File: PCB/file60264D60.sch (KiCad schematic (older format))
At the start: 43 parts, among them J8 PJ-102AH, Q1 FDD6685, Q2 2N7002K, SW0 B3F-1055, U1 LMZ22005TZ_NOPB

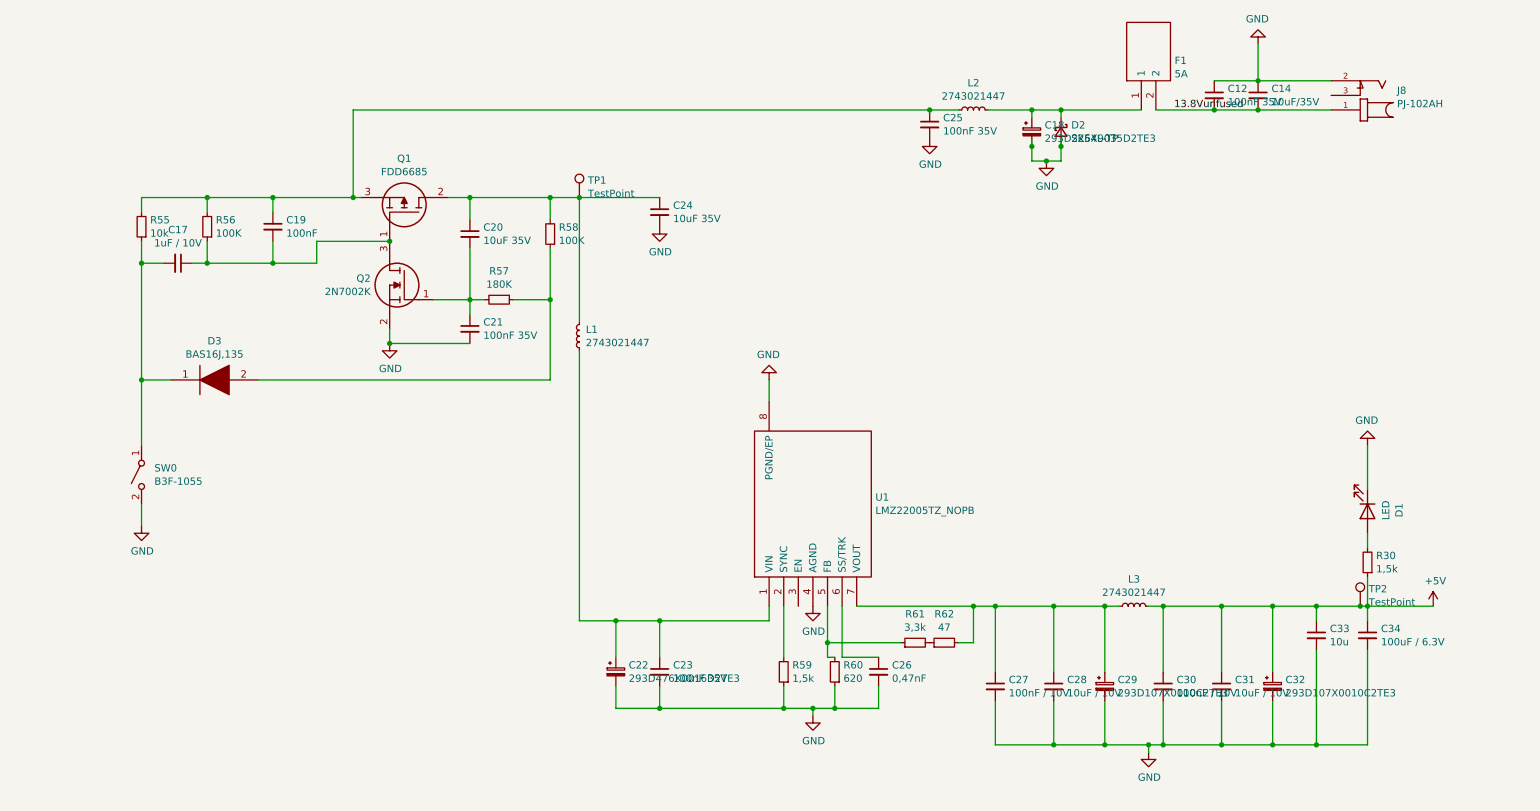
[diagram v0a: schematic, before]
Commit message: Cleaned up repository. Created a BOM in iBOM Format.
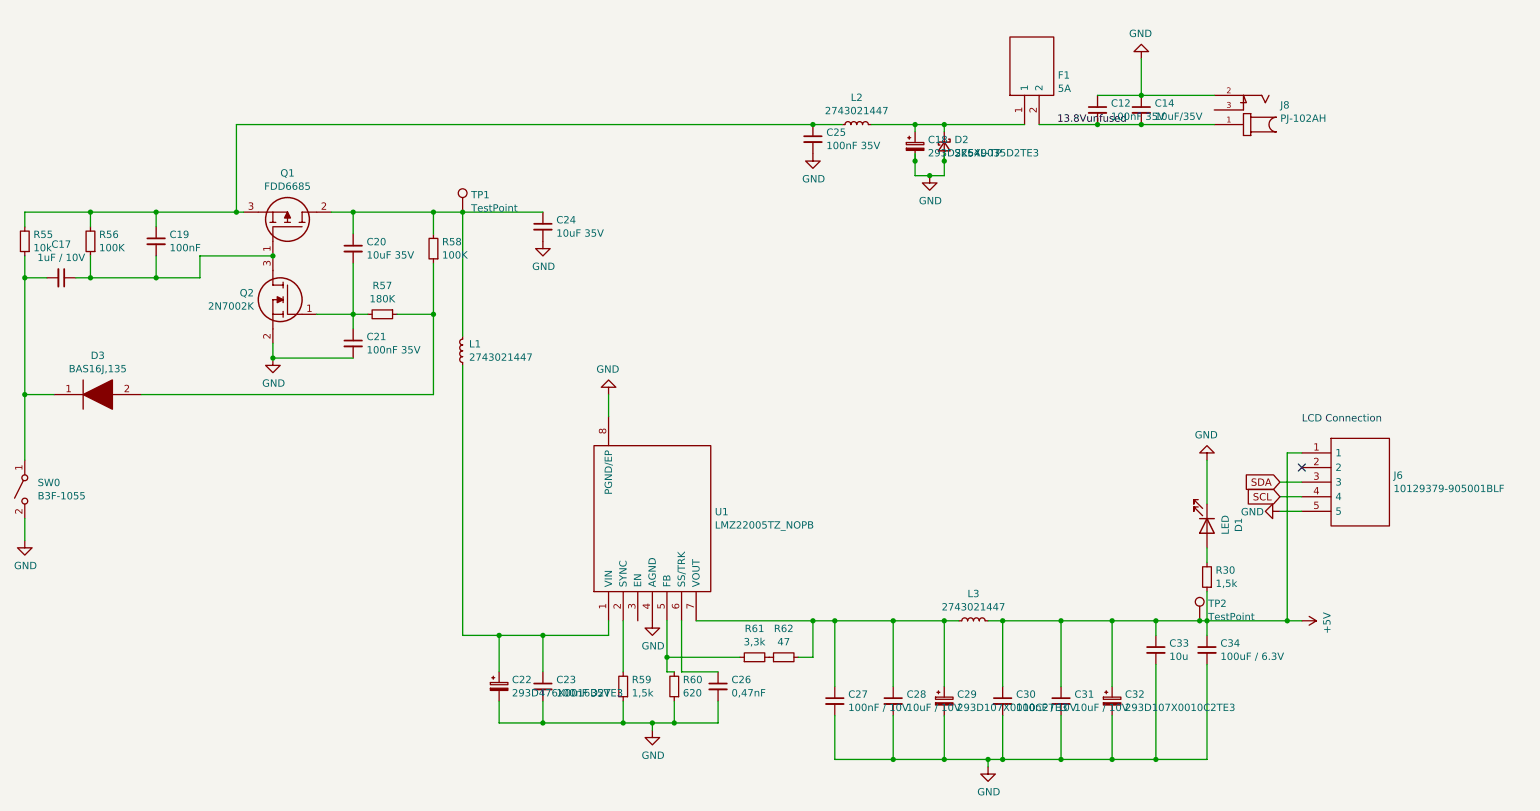
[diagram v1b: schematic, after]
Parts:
- added J6: 10129379-905001BLF, HDRRA5W67P0X254_1X5_1270X254X241P, symbol SamacSys_Parts:10129379-905001BLF
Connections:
- net +5V: now also J6.1
- net GND: now also J6.5
- new net SCL: J6.4
- new net SDA: J6.3
- no-connect marks 0 -> 1
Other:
- note added: "LCD Connection"
- moved on the sheet: C12, C14, C17, C18, C19, C20, C21, C22, C23, C24, C25, C26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

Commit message: Completed parts details on schematics and recreated gerbers and bom.
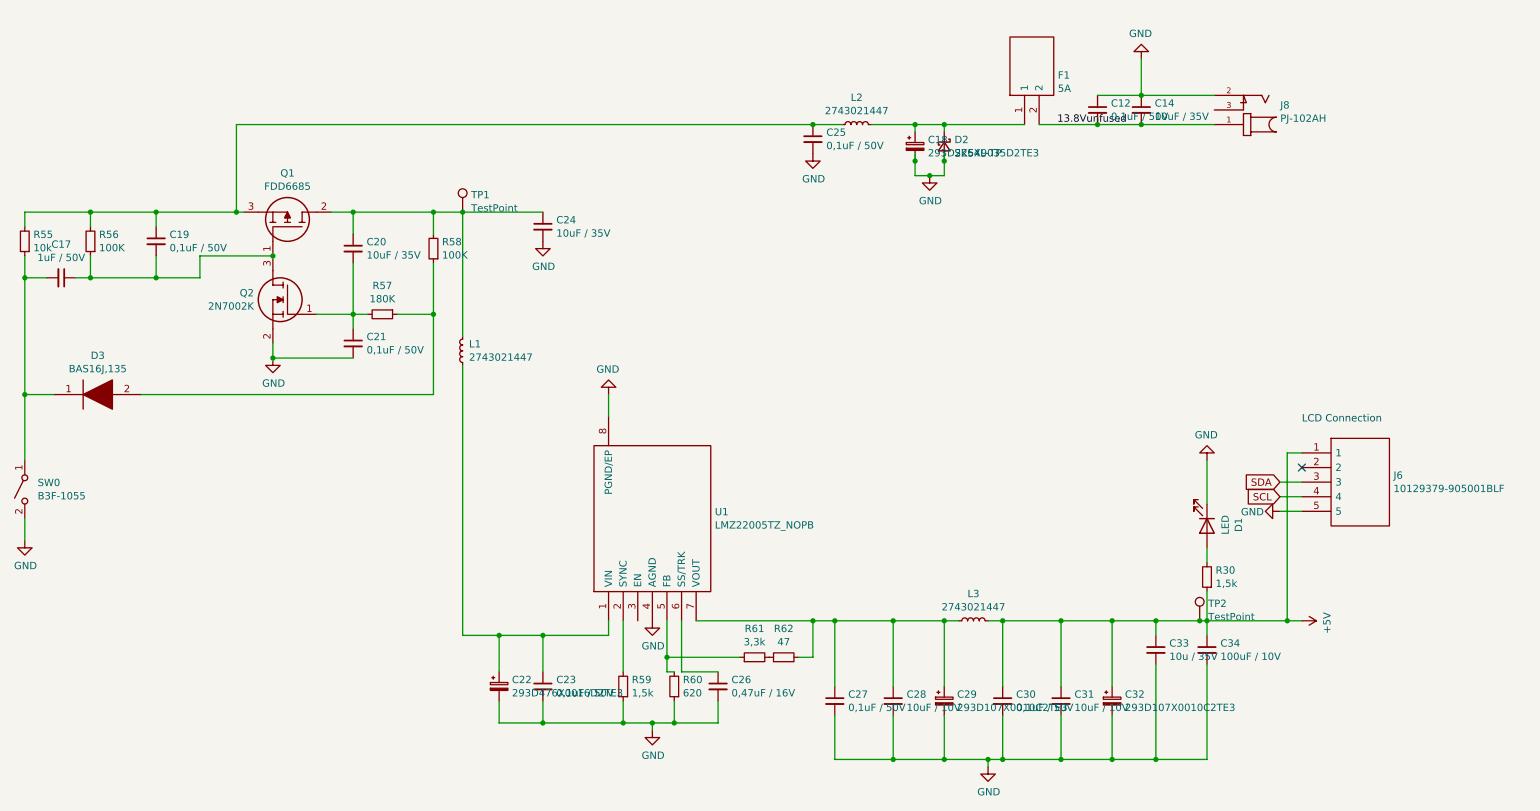
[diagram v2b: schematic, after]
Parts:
- C12, C21, C23, C25: value 100nF 35V -> 0,1uF / 50V; LCSC (none) -> C62912; Manufacturer_Name (none) -> Samsung Electro-Mechanics; Manufacturer_Part_Number (none) -> CL21B104KBCSFNC; Mouser Part Number (none) -> 187-CL21B104KBCSFNC
- C14: value 10uF/35V -> 10uF / 35V; Manufacturer_Name (none) -> Samsung Electro-Mechanics; Manufacturer_Part_Number (none) -> CL21A106KBYQNNE; Mouser Part Number (none) -> 187-CL21A106KBYQNNE
- C17: value 1uF / 10V -> 1uF / 50V; LCSC (none) -> C28323; Manufacturer_Name (none) -> Samsung Electro-Mechanics; Manufacturer_Part_Number (none) -> CL21B105KBFNNNE; Mouser Part Number (none) -> 187-CL21B105KBFNNNE
- C18: LCSC (none) -> C167035
- C19: value 100nF -> 0,1uF / 50V; LCSC (none) -> C62912; Manufacturer_Name (none) -> Samsung Electro-Mechanics; Manufacturer_Part_Number (none) -> CL21B104KBCSFNC; Mouser Part Number (none) -> 187-CL21B104KBCSFNC
- C20, C24: value 10uF 35V -> 10uF / 35V; Manufacturer_Name (none) -> Samsung Electro-Mechanics; Manufacturer_Part_Number (none) -> CL21A106KBYQNNE; Mouser Part Number (none) -> 187-CL21A106KBYQNNE
- C22: LCSC (none) -> C130385
- C26: value 0,47nF -> 0,47uF / 16V; Manufacturer_Name (none) -> Samsung Electro-Mechanics; Manufacturer_Part_Number (none) -> CL21B474KOFNNNE; Mouser Part Number (none) -> 187-CL21B474KOFNNNE
- C27, C30: value 100nF / 10V -> 0,1uF / 50V; LCSC (none) -> C62912; Manufacturer_Name (none) -> Samsung Electro-Mechanics; Manufacturer_Part_Number (none) -> CL21B104KBCSFNC; Mouser Part Number (none) -> 187-CL21B104KBCSFNC
- C28, C31: LCSC (none) -> C91245; Manufacturer_Name (none) -> Samsung Electro-Mechanics; Manufacturer_Part_Number (none) -> CL21A106MPFNNNE; Mouser Part Number (none) -> 187-CL21A106MPFNNNE
- C29, C32: LCSC (none) -> C136005
- C33: value 10u -> 10u / 35V; Manufacturer_Name (none) -> Samsung Electro-Mechanics; Manufacturer_Part_Number (none) -> CL21A106KBYQNNE; Mouser Part Number (none) -> 187-CL21A106KBYQNNE
- C34: value 100uF / 6.3V -> 100uF / 10V; footprint Capacitor_SMD:C_1210_3225Metric_Pad1.42x2.65mm_HandSolder -> Capacitor_SMD:C_0805_2012Metric_Pad1.15x1.40mm_HandSolder; LCSC (none) -> C307523; Manufacturer_Name (none) -> Samsung Electro-Mechanics; Manufacturer_Part_Number (none) -> CL21A106KPFNNNG; Mouser Part Number (none) -> 187-CL21A106KPFNNNG
- J8: Manufacturer_Name (none) -> CUI Devices; Manufacturer_Part_Number (none) -> PJ-102AH; Mouser Part Number (none) -> 490-PJ-102AH
- Q1: LCSC (none) -> C10866
- Q2: LCSC (none) -> C116584
- R30, R59: LCSC (none) -> C4310; Manufacturer_Name (none) -> Vishay; Manufacturer_Part_Number (none) -> CRCW08051K50FKEA; Mouser Part Number (none) -> 71-CRCW0805-1.5K-E3
- R55: LCSC (none) -> C17414; Manufacturer_Name (none) -> Vishay; Manufacturer_Part_Number (none) -> CRCW080510K0FKEAC; Mouser Part Number (none) -> 71-CRCW080510K0FKEAC
- R56, R58: LCSC (none) -> C17407; Manufacturer_Name (none) -> Vishay; Manufacturer_Part_Number (none) -> CRCW0805100KFKEAC; Mouser Part Number (none) -> 71-CRCW0805100KFKEAC
- R57: LCSC (none) -> C17501; Manufacturer_Name (none) -> Vishay; Manufacturer_Part_Number (none) -> CRCW0805180KFKEAC; Mouser Part Number (none) -> 71-CRCW0805180KFKEAC
- R60: LCSC (none) -> C17782; Manufacturer_Name (none) -> Vishay; Manufacturer_Part_Number (none) -> CRCW0805620RFKEA; Mouser Part Number (none) -> 71-CRCW0805620RFKEA
- R61: LCSC (none) -> C26010; Manufacturer_Name (none) -> Vishay; Manufacturer_Part_Number (none) -> CRCW08053K30FKEAC; Mouser Part Number (none) -> 71-CRCW08053K30FKEAC
- R62: LCSC (none) -> C17714; Manufacturer_Name (none) -> Vishay; Manufacturer_Part_Number (none) -> CRCW080547R0FKEAC; Mouser Part Number (none) -> 71-CRCW080547R0FKEAC
